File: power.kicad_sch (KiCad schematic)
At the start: 28 parts, among them U4 TPS54302, U5 SCT2450

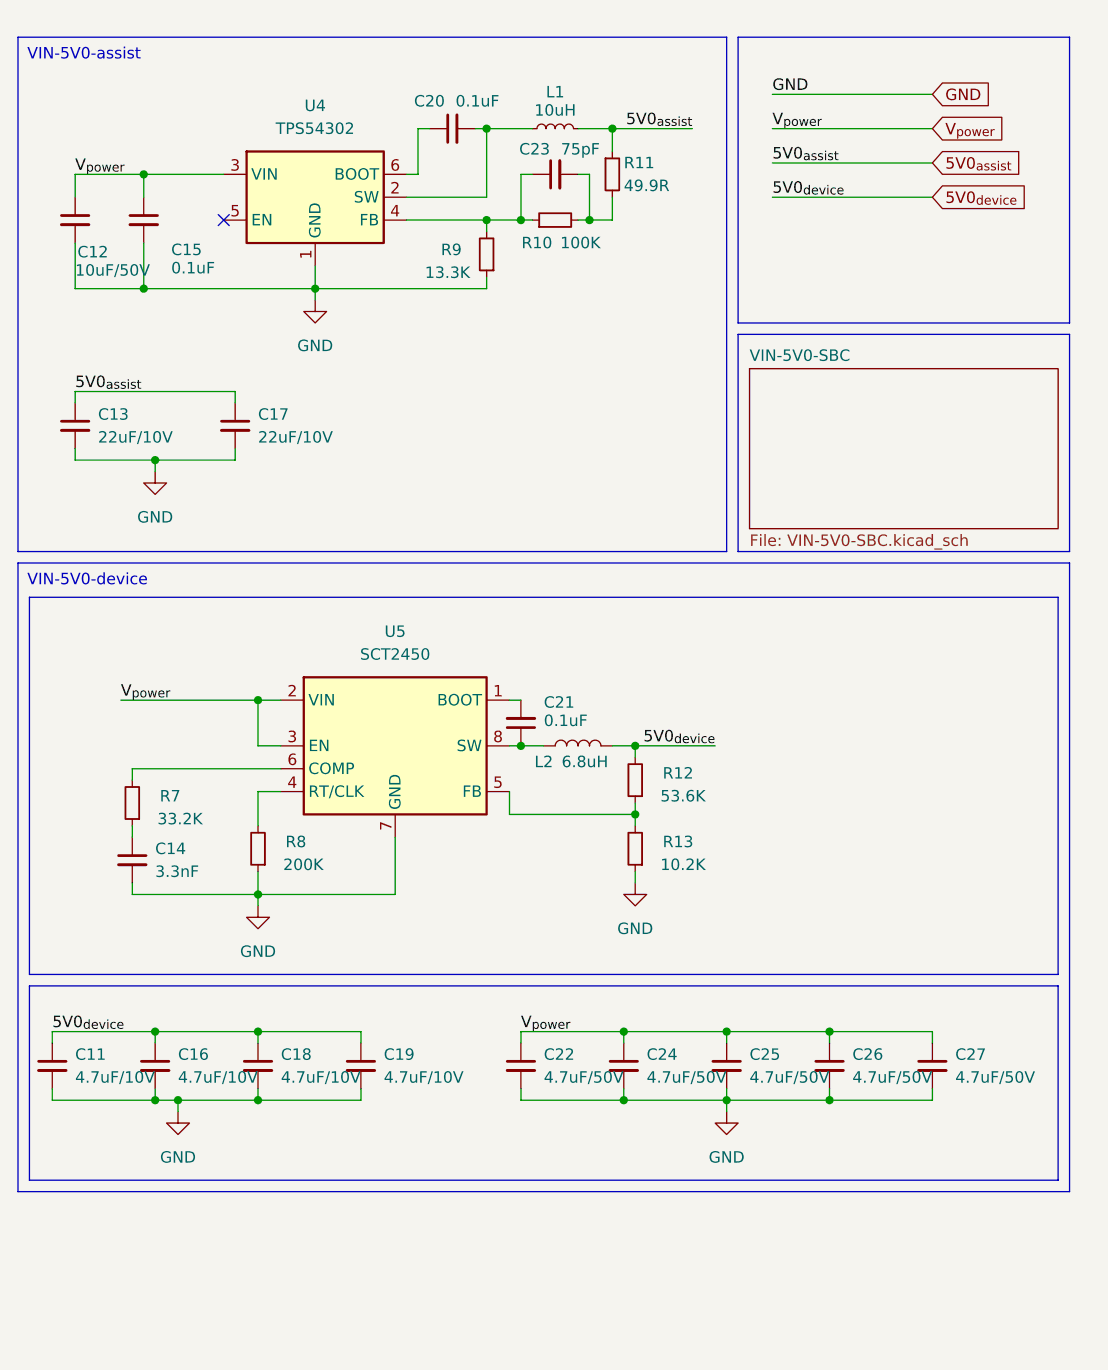
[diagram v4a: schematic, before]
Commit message: pref: USB外设改自供电，优化布线
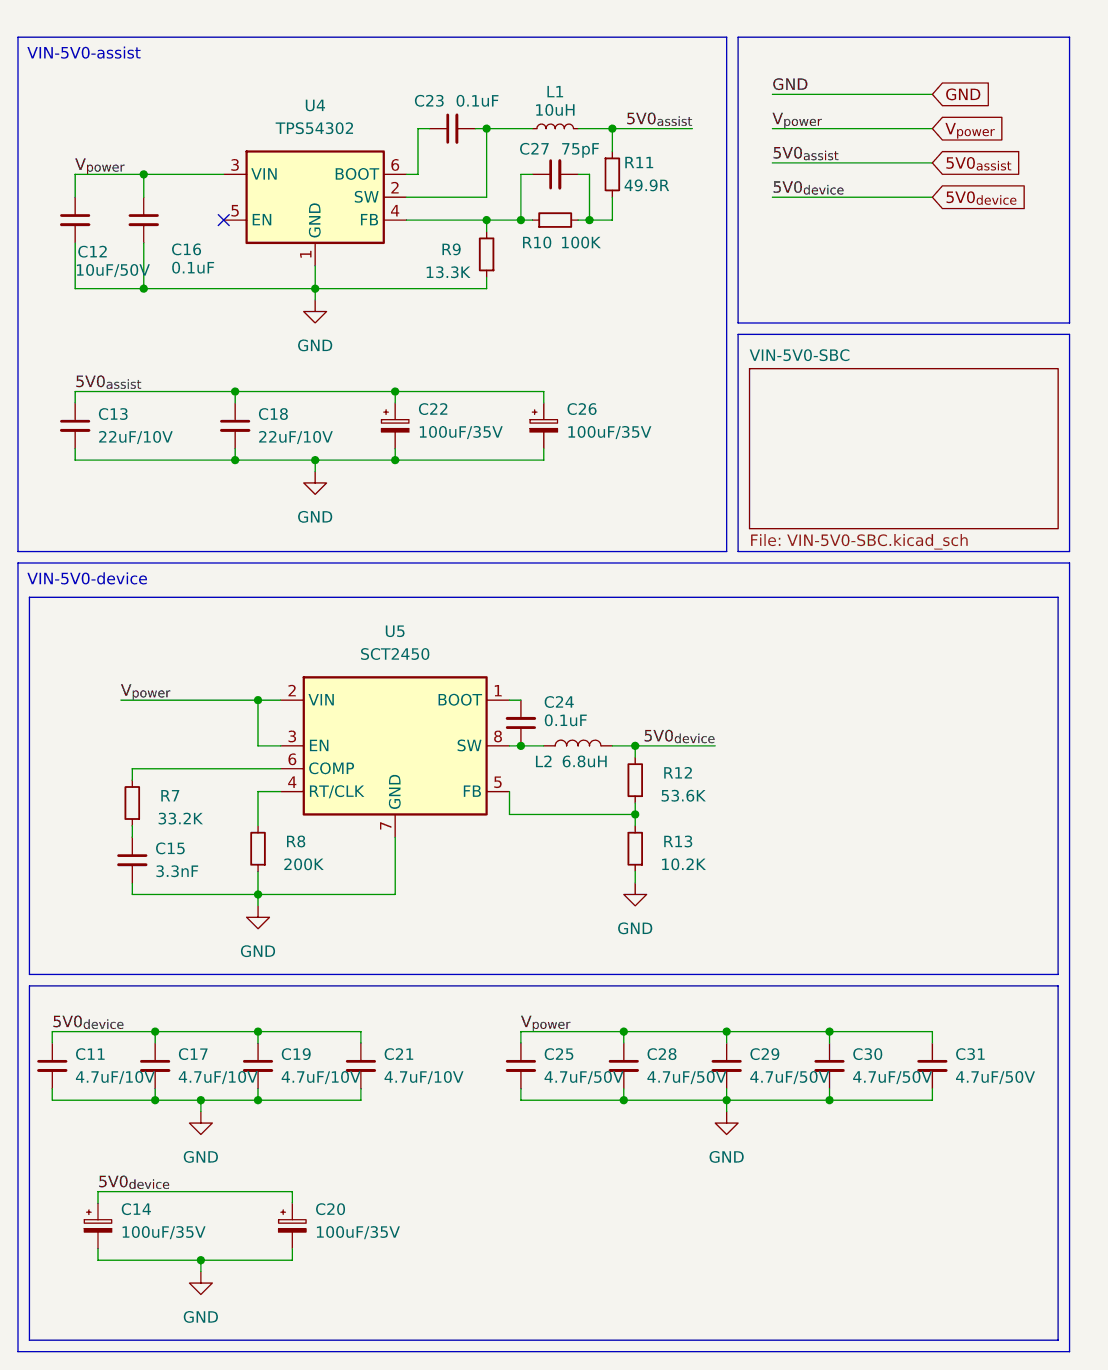
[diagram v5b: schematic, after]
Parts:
- added C14, C20, C22, C26: 100uF/35V, Capacitor_SMD:CP_Elec_6.3x7.7, symbol Device:C_Polarized_Small
- renumbered C14 to C15, C15 to C16, C16 to C17, C17 to C18, C18 to C19, C19 to C21, C20 to C23, C21 to C24, C22 to C25, C23 to C27, C24 to C28, C25 to C29, C26 to C30, C27 to C31
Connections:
- net 5V0_{assist}: now also C22.1, C26.1
- net 5V0_{device}: now also C14.1, C20.1
- net GND: now also C14.2, C20.2, C22.2, C26.2
